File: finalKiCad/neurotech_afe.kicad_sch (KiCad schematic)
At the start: 36 parts, among them J2 Conn_01x03_Socket, U1 ADS1220xPW, U2 Opamp_Quad, U3 ${SIM.PARAMS}, U4 TLV70033_SOT23-5, U7 113991054

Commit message: added final schematic
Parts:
- removed 10k? (x2): R_Small, symbol Device:R_Small
- removed 50k, 5k: R_Potentiometer_Dual, symbol Device:R_Potentiometer_Dual
- removed R10: 11k, symbol Device:R
- removed R2: 10k, symbol Device:R
- added 10k1: R_Small, symbol Device:R_Small
- added 20k1, 50k1: R_Potentiometer, symbol Device:R_Potentiometer
- added U6: Opamp_Quad, symbol Device:Opamp_Quad
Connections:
- net +3.3V: now also U6.4 (V+)
- net 1.65 V: now also 20k1.3; no longer C2.2, U2.10 (+), U2.6 (-), U2.7, U2.9 (-)
- net CS: now also U7.1 (D0)
- net GND: now also U3.3 (V+), U6.11 (V-); no longer U3.4 (V-)
- net IAout: now also C3.1; no longer R1.1
- net Reference_Electrode: now also R17.2
- net Vout: now also C2.2, U2.9 (-)
- net at C1.1: now also R1.2, 50k1.1
- net at U2.1, U2.2 (-): now also R1.1, 10k1.2; no longer C1.2, C3.1
- net at U2.3 (+): now also C4.2, 20k1.2; no longer C2.1
- net at C3.2, C4.1: now also 10k1.1
- net at U2.5 (+): now also C2.1, 50k1.2; no longer C4.2
- removed net 1.65V: R17.2, U3.3 (V+)
- new net: C1.2, U2.10 (+), U2.6 (-), U2.7
- new net +3V3: U3.4 (V-)
- no-connect marks 11 -> 9
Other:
- note removed: "what if we put actual pots instead of digipots"
- moved on the sheet: C1, C2, C3, C4, C8, C9, R1, R5, U4

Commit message: fixed ERC errors
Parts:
- removed J2: Conn_01x03_Socket, symbol Connector:Conn_01x03_Socket
- removed U6: Opamp_Quad, symbol Device:Opamp_Quad
- added C12: 100nF, symbol Device:C
- added TP1, TP2, TP3: TestPoint, symbol Connector:TestPoint
- gave numbers to parts that had none: 2
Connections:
- net VREF is gone; now on net +3.3V: U1.10 (AIN1)
- net +3.3V: now also C12.1
- net 1.65 V: now also 20k1.1
- net GND: now also C12.2
- net Negative_Electrode: now also TP1.1
- net Positive_Electrode: now also TP2.1
- net Reference_Electrode: now also TP3.1
- no-connect marks 9 -> 14
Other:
- note removed: "sean: added decoupling caps (said so on ad688 datasheet)"
- moved on the sheet: R12, R13, R17

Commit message: assigned passive footprints
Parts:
- 10k1, R1, R12, R13, R17, R2, R4, R5: footprint (none) -> Resistor_SMD:R_0201_0603Metric_Pad0.64x0.40mm_HandSolder
- C1, C10, C11, C12, C2, C3, C4, C5, C6, C7, C8, C9: footprint (none) -> Capacitor_SMD:C_0201_0603Metric_Pad0.64x0.40mm_HandSolder
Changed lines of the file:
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@@
 			)
 		)
-		(property "Footprint" ""
+		(property "Footprint" "Capacitor_SMD:C_0201_0603Metric_Pad0.64x0.40mm_HandSolder"
 			(at 332.74 28.2448 0)
 			(effects
@@
 			)
 		)
-		(property "Footprint" ""
+		(property "Footprint" "Capacitor_SMD:C_0201_0603Metric_Pad0.64x0.40mm_HandSolder"
 			(at 251.46 39.6748 0)
 			(effects
@@
 			)
 		)
-		(property "Footprint" ""
+		(property "Footprint" "Capacitor_SMD:C_0201_0603Metric_Pad0.64x0.40mm_HandSolder"
 			(at 65.7352 208.28 0)
 			(effects
@@
 			)
 		)
-		(property "Footprint" ""
+		(property "Footprint" "Resistor_SMD:R_0201_0603Metric_Pad0.64x0.40mm_HandSolder"
 			(at 51.562 104.14 90)
 			(effects
@@
 			)
 		)
-		(property "Footprint" ""
+		(property "Footprint" "Capacitor_SMD:C_0201_0603Metric_Pad0.64x0.40mm_HandSolder"
 			(at 129.2352 74.93 0)
 			(effects
@@
 			)
 		)
-		(property "Footprint" ""
+		(property "Footprint" "Resistor_SMD:R_0201_0603Metric_Pad0.64x0.40mm_HandSolder"
 			(at 77.47 129.032 90)
 			(effects
@@
 			)
 		)
-		(property "Footprint" ""
+		(property "Footprint" "Capacitor_SMD:C_0201_0603Metric_Pad0.64x0.40mm_HandSolder"
 			(at 27.6352 106.68 0)
 			(effects
@@
 			)
 		)
-		(property "Footprint" ""
+		(property "Footprint" "Resistor_SMD:R_0201_0603Metric_Pad0.64x0.40mm_HandSolder"
 			(at 184.658 44.45 90)
 			(effects
@@
 			)
 		)
-		(property "Footprint" ""
+		(property "Footprint" "Capacitor_SMD:C_0201_0603Metric_Pad0.64x0.40mm_HandSolder"
 			(at 332.4352 143.51 0)
 			(effects
@@
 			)
 		)
-		(property "Footprint" ""
+		(property "Footprint" "Resistor_SMD:R_0201_0603Metric_Pad0.64x0.40mm_HandSolder"
 			(at 295.91 44.958 90)
 			(effects
@@
 			)
 		)
-		(property "Footprint" ""
+		(property "Footprint" "Capacitor_SMD:C_0201_0603Metric_Pad0.64x0.40mm_HandSolder"
 			(at 33.9852 208.28 0)
 			(effects
@@
 			)
 		)
-		(property "Footprint" ""
+		(property "Footprint" "Capacitor_SMD:C_0201_0603Metric_Pad0.64x0.40mm_HandSolder"
 			(at 332.4352 53.34 0)
 			(effects
@@
 			)
 		)
-		(property "Footprint" ""
+		(property "Footprint" "Resistor_SMD:R_0201_0603Metric_Pad0.64x0.40mm_HandSolder"
 			(at 247.65 31.75 0)
 			(effects
@@
 			)
 		)
-		(property "Footprint" ""
+		(property "Footprint" "Capacitor_SMD:C_0201_0603Metric_Pad0.64x0.40mm_HandSolder"
 			(at 139.3952 74.93 0)
 			(effects
@@
 			)
 		)
-		(property "Footprint" ""
+		(property "Footprint" "Resistor_SMD:R_0201_0603Metric_Pad0.64x0.40mm_HandSolder"
 			(at 51.562 111.76 90)
 			(effects
@@
 			)
 		)
-		(property "Footprint" ""
+		(property "Footprint" "Capacitor_SMD:C_0201_0603Metric_Pad0.64x0.40mm_HandSolder"
 			(at 342.5952 160.02 0)
 			(effects
@@
 			)
 		)
-		(property "Footprint" ""
+		(property "Footprint" "Resistor_SMD:R_0201_0603Metric_Pad0.64x0.40mm_HandSolder"
 			(at 59.69 144.272 90)
 			(effects
@@
 			)
 		)
-		(property "Footprint" ""
+		(property "Footprint" "Capacitor_SMD:C_0201_0603Metric_Pad0.64x0.40mm_HandSolder"
 			(at 87.3252 58.42 0)
 			(effects
@@
 			)
 		)
-		(property "Footprint" ""
+		(property "Footprint" "Resistor_SMD:R_0201_0603Metric_Pad0.64x0.40mm_HandSolder"
 			(at 91.44 107.188 90)
 			(effects
@@
 			)
 		)
-		(property "Footprint" ""
+		(property "Footprint" "Capacitor_SMD:C_0201_0603Metric_Pad0.64x0.40mm_HandSolder"
 			(at 243.84 39.6748 0)
 			(effects

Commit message: cleaned up schm
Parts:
- removed R4, R5: R, Resistor_SMD:R_0201_0603Metric_Pad0.64x0.40mm_HandSolder, symbol Device:R
- removed RN3: 3.3k, symbol Device:R_Pack02
- removed U3: ${SIM.PARAMS}, symbol Simulation_SPICE:OPAMP
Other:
- moved on the sheet: 10k1, 20k1, 50k1, C1, C10, C11, C2, C3, C4, R1, U1, U2A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

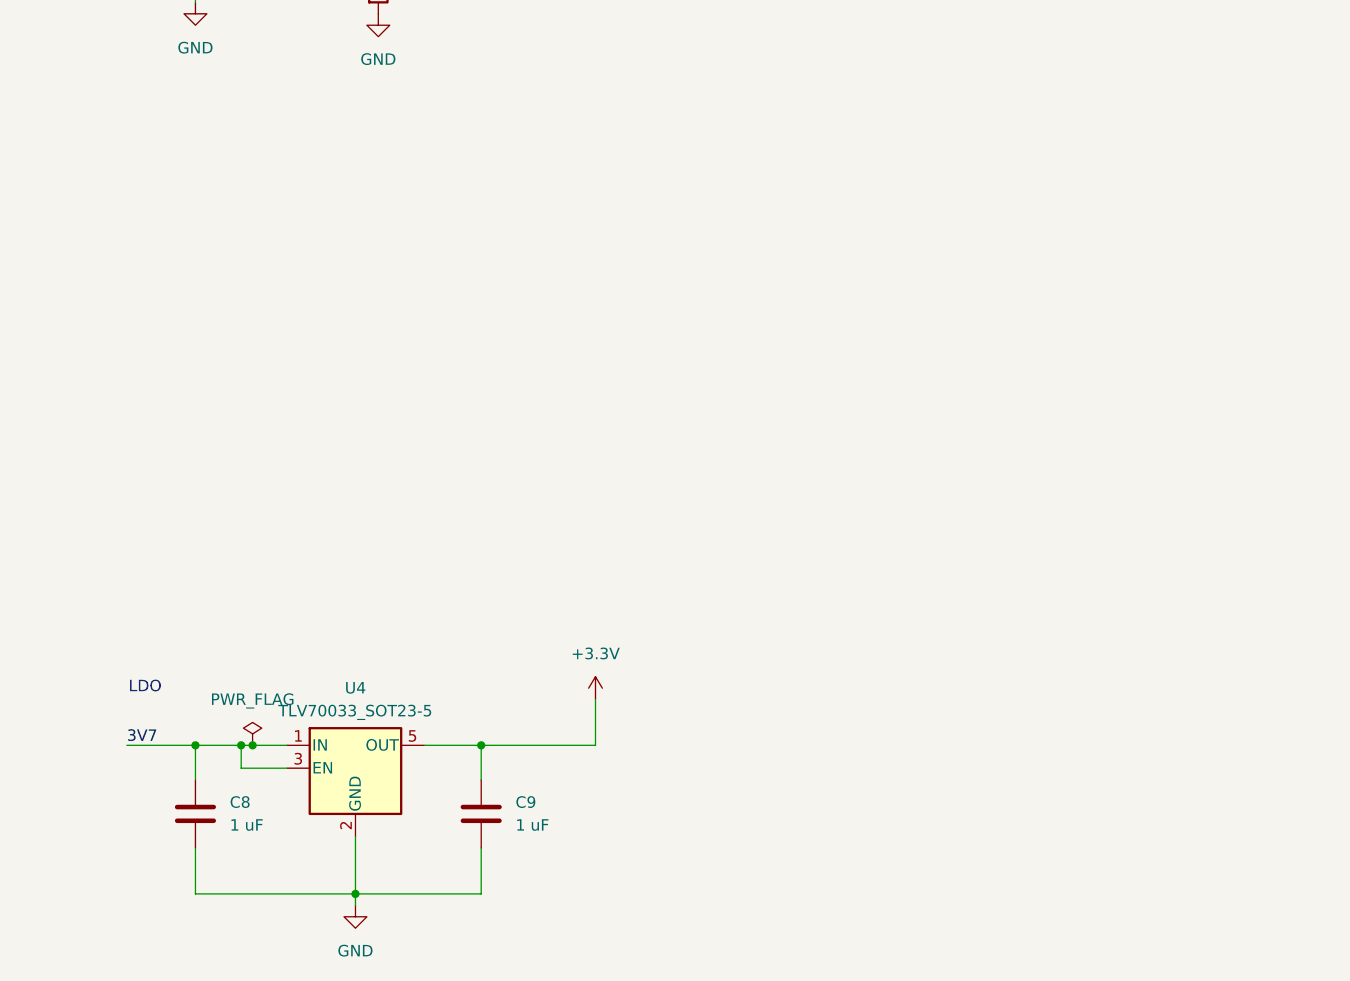
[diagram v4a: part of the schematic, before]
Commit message: Created pcb layout and started wiring
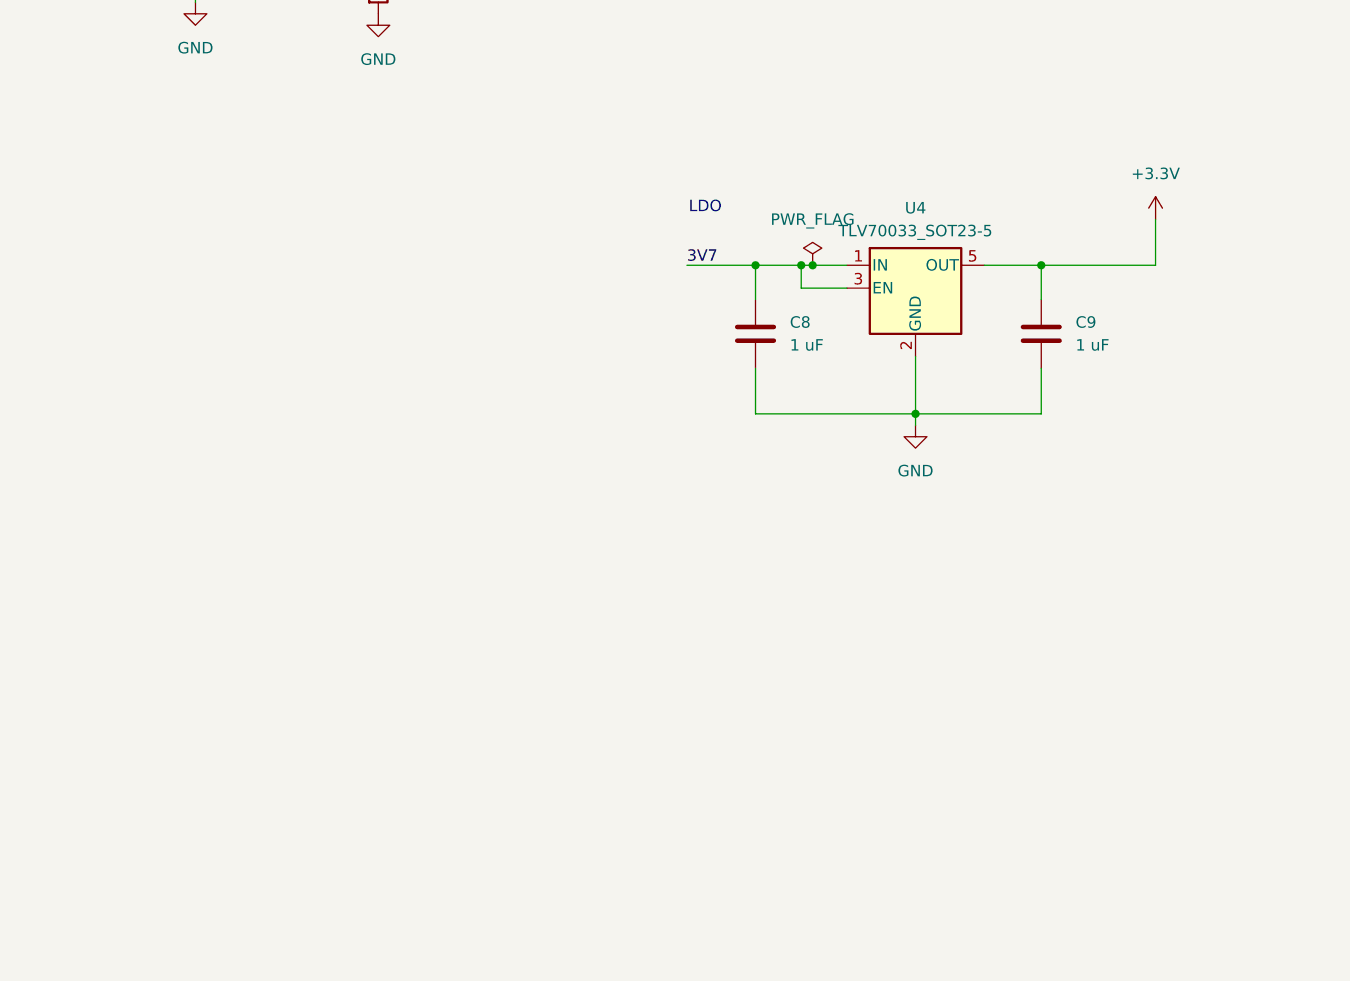
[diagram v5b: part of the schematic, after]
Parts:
- 20k1, 50k1: footprint (none) -> Potentiometer_THT:Potentiometer_Bourns_3362P_Vertical
- RN1, RN2: footprint (none) -> ResistorArray_SMD:R_Array_Convex_4x0805
- TP1, TP2, TP3: footprint (none) -> TestPoint:TestPoint_THTPad_D2.0mm_Drill1.0mm
- U2: footprint (none) -> Package_SO:SOIC-14_3.9x8.7mm_P1.27mm
- U5: footprint R_8_ADI -> Package_SO:SOIC-8_3.9x4.9mm_P1.27mm
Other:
- moved on the sheet: C8, C9, U4

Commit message: reassigned footprints and values
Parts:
- C1, C10, C11, C12, C2, C3, C4, C5, C6, C8, C9: footprint Capacitor_SMD:C_0201_0603Metric_Pad0.64x0.40mm_HandSolder -> Capacitor_SMD:C_0603_1608Metric_Pad1.08x0.95mm_HandSolder
- C7: value C -> 4.7n; footprint Capacitor_SMD:C_0201_0603Metric_Pad0.64x0.40mm_HandSolder -> Capacitor_SMD:C_0603_1608Metric_Pad1.08x0.95mm_HandSolder
- R1, R12, R13, R17, R2: footprint Resistor_SMD:R_0201_0603Metric_Pad0.64x0.40mm_HandSolder -> Resistor_SMD:R_0603_1608Metric_Pad0.98x0.95mm_HandSolder
- R3: renamed from 10k1; value R_Small -> 10k; footprint Resistor_SMD:R_0201_0603Metric_Pad0.64x0.40mm_HandSolder -> Resistor_SMD:R_0603_1608Metric_Pad0.98x0.95mm_HandSolder
- R_Pot1: renamed from 20k1; value R_Potentiometer -> 20k
- R_Pot2: renamed from 50k1; value R_Potentiometer -> 50k
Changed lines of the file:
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@@
 			)
 		)
-		(property "Footprint" "Capacitor_SMD:C_0201_0603Metric_Pad0.64x0.40mm_HandSolder"
+		(property "Footprint" "Capacitor_SMD:C_0603_1608Metric_Pad1.08x0.95mm_HandSolder"
 			(at 306.07 30.7848 0)
 			(effects
@@
 			)
 		)
-		(property "Footprint" "Capacitor_SMD:C_0201_0603Metric_Pad0.64x0.40mm_HandSolder"
+		(property "Footprint" "Capacitor_SMD:C_0603_1608Metric_Pad1.08x0.95mm_HandSolder"
 			(at 224.79 42.2148 0)
 			(effects
@@
 			)
 		)
-		(property "Footprint" "Capacitor_SMD:C_0201_0603Metric_Pad0.64x0.40mm_HandSolder"
+		(property "Footprint" "Capacitor_SMD:C_0603_1608Metric_Pad1.08x0.95mm_HandSolder"
 			(at 127.9652 154.94 0)
 			(effects
@@
 			)
 		)
-		(property "Footprint" "Resistor_SMD:R_0201_0603Metric_Pad0.64x0.40mm_HandSolder"
+		(property "Footprint" "Resistor_SMD:R_0603_1608Metric_Pad0.98x0.95mm_HandSolder"
 			(at 51.562 104.14 90)
 			(effects
@@
 			)
 		)
-		(property "Footprint" "Capacitor_SMD:C_0201_0603Metric_Pad0.64x0.40mm_HandSolder"
+		(property "Footprint" "Capacitor_SMD:C_0603_1608Metric_Pad1.08x0.95mm_HandSolder"
 			(at 129.2352 74.93 0)
 			(effects
@@
 			)
 		)
-		(property "Footprint" "Capacitor_SMD:C_0201_0603Metric_Pad0.64x0.40mm_HandSolder"
+		(property "Footprint" "Capacitor_SMD:C_0603_1608Metric_Pad1.08x0.95mm_HandSolder"
 			(at 27.6352 106.68 0)
 			(effects
@@
 			)
 		)
-		(property "Footprint" "Resistor_SMD:R_0201_0603Metric_Pad0.64x0.40mm_HandSolder"
+		(property "Footprint" "Resistor_SMD:R_0603_1608Metric_Pad0.98x0.95mm_HandSolder"
 			(at 184.658 44.45 90)
 			(effects
@@
 			)
 		)
-		(property "Footprint" "Capacitor_SMD:C_0201_0603Metric_Pad0.64x0.40mm_HandSolder"
+		(property "Footprint" "Capacitor_SMD:C_0603_1608Metric_Pad1.08x0.95mm_HandSolder"
 			(at 262.5852 105.41 0)
 			(effects
@@
 		(dnp no)
 		(fields_autoplaced yes)
-		(property "Reference" "50k1"
+		(property "Reference" "R_Pot2"
 			(at 283.21 44.4499 0)
 			(effects
@@
 			)
 		)
-		(property "Value" "R_Potentiometer"
+		(property "Value" "50k"
 			(at 283.21 46.9899 0)
 			(effects
@@
 			(project "neurotech_afe"
 				(path "/d657415d-773f-4d61-9200-85fede9d1019"
-					(reference "50k1")
+					(reference "R_Pot2")
 					(unit 1)
 				)
@@
 			)
 		)
-		(property "Footprint" "Resistor_SMD:R_0201_0603Metric_Pad0.64x0.40mm_HandSolder"
+		(property "Footprint" "Resistor_SMD:R_0603_1608Metric_Pad0.98x0.95mm_HandSolder"
 			(at 269.24 47.498 90)
 			(effects
@@
 			)
 		)
-		(property "Footprint" "Capacitor_SMD:C_0201_0603Metric_Pad0.64x0.40mm_HandSolder"
+		(property "Footprint" "Capacitor_SMD:C_0603_1608Metric_Pad1.08x0.95mm_HandSolder"
 			(at 96.2152 154.94 0)
 			(effects
@@
 			)
 		)
-		(property "Footprint" "Capacitor_SMD:C_0201_0603Metric_Pad0.64x0.40mm_HandSolder"
+		(property "Footprint" "Capacitor_SMD:C_0603_1608Metric_Pad1.08x0.95mm_HandSolder"
 			(at 305.7652 55.88 0)
 			(effects
@@
 		(on_board yes)
 		(dnp no)
-		(property "Reference" "20k1"
+		(property "Reference" "R_Pot1"
 			(at 227.33 44.4501 0)
 			(effects
@@
 			)
 		)
-		(property "Value" "R_Potentiometer"
+		(property "Value" "20k"
 			(at 227.33 41.9101 0)
 			(effects
@@
 			(project "neurotech_afe"
 				(path "/d657415d-773f-4d61-9200-85fede9d1019"
-					(reference "20k1")
+					(reference "R_Pot1")
 					(unit 1)
 				)
@@
 		(dnp no)
 		(fields_autoplaced yes)
-		(property "Reference" "10k1"
+		(property "Reference" "R3"
 			(at 220.98 29.21 90)
 			(effects
@@
 			)
 		)
-		(property "Value" "R_Small"
+		(property "Value" "10k"
 			(at 220.98 31.75 90)
 			(effects
@@
 			)
 		)
-		(property "Footprint" "Resistor_SMD:R_0201_0603Metric_Pad0.64x0.40mm_HandSolder"
+		(property "Footprint" "Resistor_SMD:R_0603_1608Metric_Pad0.98x0.95mm_HandSolder"
 			(at 220.98 34.29 0)
 			(effects
@@
 			(project "neurotech_afe"
 				(path "/d657415d-773f-4d61-9200-85fede9d1019"
-					(reference "10k1")
+					(reference "R3")
 					(unit 1)
 				)
@@
 			)
 		)
-		(property "Footprint" "Capacitor_SMD:C_0201_0603Metric_Pad0.64x0.40mm_HandSolder"
+		(property "Footprint" "Capacitor_SMD:C_0603_1608Metric_Pad1.08x0.95mm_HandSolder"
 			(at 139.3952 74.93 0)
 			(effects
@@
 			)
 		)
-		(property "Footprint" "Resistor_SMD:R_0201_0603Metric_Pad0.64x0.40mm_HandSolder"
+		(property "Footprint" "Resistor_SMD:R_0603_1608Metric_Pad0.98x0.95mm_HandSolder"
 			(at 51.562 111.76 90)
 			(effects
@@
 			)
 		)
-		(property "Footprint" "Capacitor_SMD:C_0201_0603Metric_Pad0.64x0.40mm_HandSolder"
+		(property "Footprint" "Capacitor_SMD:C_0603_1608Metric_Pad1.08x0.95mm_HandSolder"
 			(at 272.7452 121.92 0)
 			(effects
@@
 			)
 		)
-		(property "Value" "C"
+		(property "Value" "4.7n"
 			(at 87.122 52.578 0)
 			(effects
@@
 			)
 		)
-		(property "Footprint" "Capacitor_SMD:C_0201_0603Metric_Pad0.64x0.40mm_HandSolder"
+		(property "Footprint" "Capacitor_SMD:C_0603_1608Metric_Pad1.08x0.95mm_HandSolder"
 			(at 87.3252 58.42 0)
 			(effects
@@
 			)
 		)
-		(property "Footprint" "Resistor_SMD:R_0201_0603Metric_Pad0.64x0.40mm_HandSolder"
+		(property "Footprint" "Resistor_SMD:R_0603_1608Metric_Pad0.98x0.95mm_HandSolder"
 			(at 91.44 107.188 90)
 			(effects
@@
 			)
 		)
-		(property "Footprint" "Capacitor_SMD:C_0201_0603Metric_Pad0.64x0.40mm_HandSolder"
+		(property "Footprint" "Capacitor_SMD:C_0603_1608Metric_Pad1.08x0.95mm_HandSolder"
 			(at 217.17 42.2148 0)
 			(effects

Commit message: Update schematic, symbols, and footprints
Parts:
- removed D1, D2: BAT54S, Package_TO_SOT_SMD:SOT-23, symbol Diode:BAT54S
- added R?: 3.3k, symbol Device:R_Small_US
- added U?: MCP4141T-103E/SN, SOIC8-N_MC_MCH, symbol Flex-Emg:MCP4141T-103E_SN
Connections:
- net +3.3V: now also U?.4
- net DIN: now also U?.3
- net SCLK: now also U?.2
- net Vout: now also U?.6; no longer C2.2, U2.9 (-)
- net CS1: now reaches U7.3 (D2)
- net CS1: now also U?.1
- new net: R?.1, U2.9 (-)
- new net: R?.2, U?.7
- new net 1.65V: C2.2
- no-connect marks 14 -> 15
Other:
- moved on the sheet: C8, C9, U4

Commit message: footprints and started layout
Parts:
- removed RN1: 3.3k, ResistorArray_SMD:R_Array_Convex_4x0805, symbol Device:R_Pack02
- removed RN2: 1M, ResistorArray_SMD:R_Array_Convex_4x0805, symbol Device:R_Pack02
- removed R_Pot1: 20k, Potentiometer_THT:Potentiometer_Bourns_3362P_Vertical, symbol Device:R_Potentiometer
- removed R_Pot2: 50k, Potentiometer_THT:Potentiometer_Bourns_3362P_Vertical, symbol Device:R_Potentiometer
- added J1: Conn_01x02_Pin, Flex-EMG:BATT_CONN, symbol Connector:Conn_01x02_Pin
- added R5: 20k, Flex-EMG:POT_PTN16-A20120K1B1, symbol Flex-Emg:PTN16-A20120K1B1
- added R6: 50k, Flex-EMG:POT_PTN16-A20120K1B1, symbol Flex-Emg:PTN16-A20120K1B1
- added U6: EXB24V332JX, Flex-EMG:C_ARRAY_EXB24V_PAN, symbol Flex-Emg:EXB24V332JX
- added U8: EXB34V105JV, Flex-EMG:C_ARRAY_EXB34V_PAN, symbol Flex-Emg:EXB34V105JV
- R4: renamed from R?; footprint (none) -> Resistor_SMD:R_0201_0603Metric_Pad0.64x0.40mm_HandSolder
- TP1, TP2, TP3: footprint TestPoint:TestPoint_THTPad_D2.0mm_Drill1.0mm -> TestPoint:TestPoint_THTPad_D4.0mm_Drill2.0mm
- U1: footprint Package_SO:TSSOP-16_4.4x5mm_P0.65mm -> Flex-EMG:SOP65P640X120-16N
- U2: footprint Package_SO:SOIC-14_3.9x8.7mm_P1.27mm -> Flex-EMG:SOP65P640X120-14N
- U3: renamed from U?; footprint SOIC8-N_MC_MCH -> Flex-EMG:SOIC8-N_MC_MCH
- U7: footprint 113991054:MODULE_113991054 -> Flex-EMG:ESP32C3
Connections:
- net 1.65V is gone; now on net 1.65 V: C2.2
- net 1.65 V: now also R5.1, U8.3, U8.4
- net 3V7: now also J1.1 (Pin_1)
- net GND: now also J1.2 (Pin_2)
- net In+: now also U6.3, U8.2
- net In-: now also U6.4, U8.1
- net Negative_Electrode: now also U6.1
- net Positive_Electrode: now also U6.2
- net at C1.1, R1.2: now also R6.3
- net at C4.2, U2.3 (+): now also R5.2
- net at C2.1, U2.5 (+): now also R6.2
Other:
- note removed: "this initial resistor could increase the thermal noise, and doesn't limit current back to the body"
- moved on the sheet: C8, C9, U4
